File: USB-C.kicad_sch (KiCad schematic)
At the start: 6 parts, among them J2 HRO_TYPE-C-31-M-12, U3 SRV05-4

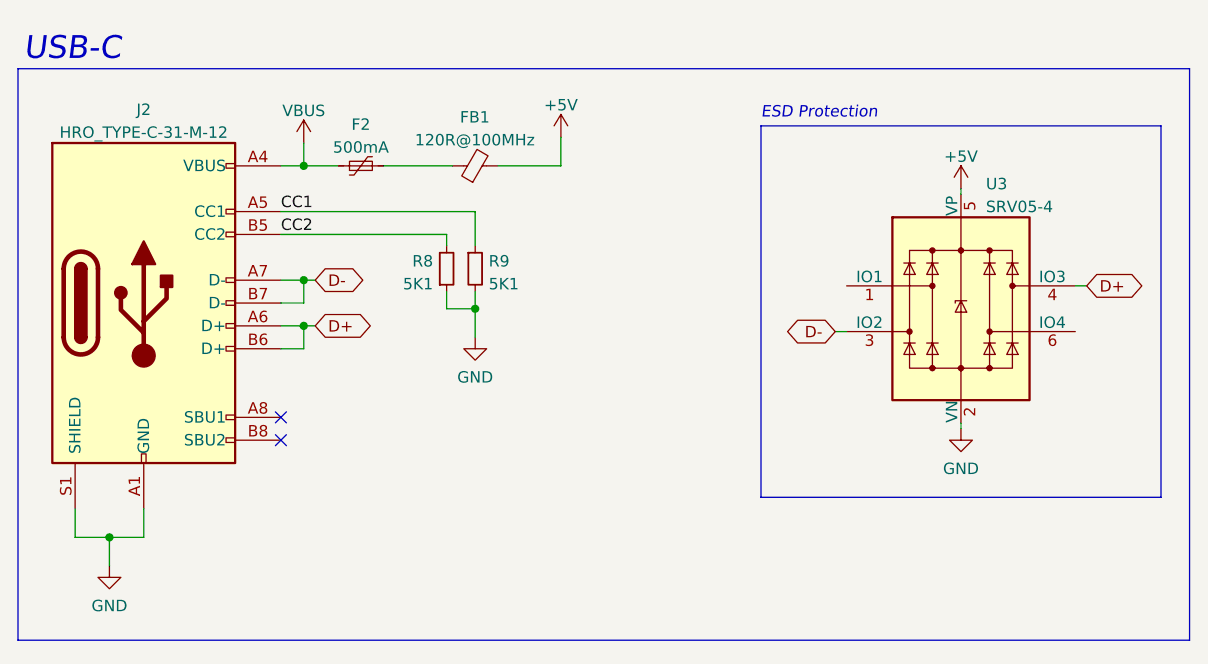
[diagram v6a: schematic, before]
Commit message: feat(schematic): Add titles and individual sheet comments
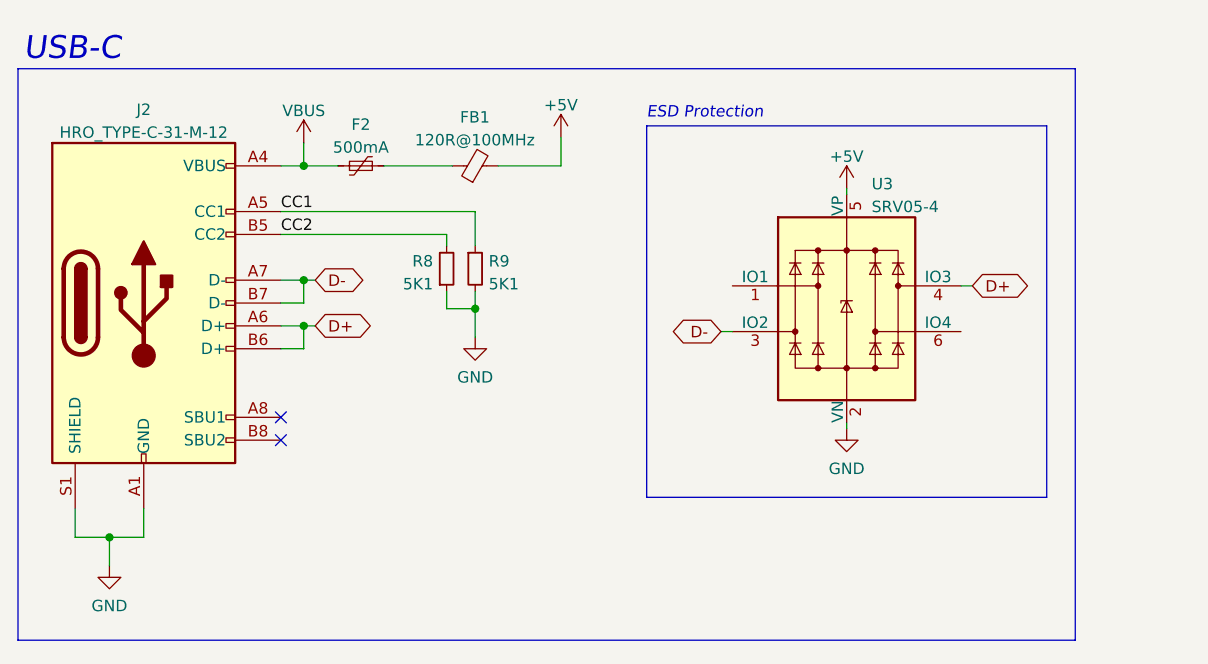
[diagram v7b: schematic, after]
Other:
- company: (none) -> Kurtis Lew
- title: (none) -> Conejo nRF52840 Keyboard - USB-C
- moved on the sheet: U3
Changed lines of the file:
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@@
 (kicad_sch (version 20211123) (generator eeschema)
   (paper "USLetter")
+  (title_block
+    (title "Conejo nRF52840 Keyboard - USB-C")
+    (company "Kurtis Lew")
+  )
   (junction (at 44.45 47.625) (diameter 0) (color 0 0 0 0)
   )
@@
   (no_connect (at 41.91 60.325))
   (no_connect (at 41.91 57.785))
-  (polyline (pts (xy 139.7 25.4) (xy 139.7 66.675))
-    (stroke (width 0) (type default) (color 0 0 0 0))
-  )
-  (wire (pts (xy 117.475 58.42) (xy 117.475 59.055))
+  (polyline (pts (xy 127 25.4) (xy 127 66.675))
+    (stroke (width 0) (type default) (color 0 0 0 0))
+  )
+  (wire (pts (xy 104.775 58.42) (xy 104.775 59.055))
     (stroke (width 0) (type default) (color 0 0 0 0))
   )
@@
     (stroke (width 0) (type default) (color 0 0 0 0))
   )
-  (wire (pts (xy 130.175 43.18) (xy 131.445 43.18))
-    (stroke (width 0) (type default) (color 0 0 0 0))
-  )
-  (polyline (pts (xy 142.875 19.05) (xy 142.875 82.55))
+  (wire (pts (xy 117.475 43.18) (xy 118.745 43.18))
+    (stroke (width 0) (type default) (color 0 0 0 0))
+  )
+  (polyline (pts (xy 130.175 19.05) (xy 130.175 82.55))
     (stroke (width 0) (type default) (color 0 0 0 0))
   )
@@
     (stroke (width 0) (type default) (color 0 0 0 0))
   )
-  (polyline (pts (xy 142.875 82.55) (xy 12.7 82.55))
+  (polyline (pts (xy 130.175 82.55) (xy 12.7 82.55))
     (stroke (width 0) (type default) (color 0 0 0 0))
   )
@@
     (stroke (width 0) (type default) (color 0 0 0 0))
   )
-  (polyline (pts (xy 95.25 66.675) (xy 95.25 25.4))
+  (polyline (pts (xy 82.55 66.675) (xy 82.55 25.4))
     (stroke (width 0) (type default) (color 0 0 0 0))
   )
@@
     (stroke (width 0) (type default) (color 0 0 0 0))
   )
-  (wire (pts (xy 104.775 48.26) (xy 103.505 48.26))
+  (wire (pts (xy 92.075 48.26) (xy 90.805 48.26))
     (stroke (width 0) (type default) (color 0 0 0 0))
   )
@@
     (stroke (width 0) (type default) (color 0 0 0 0))
   )
-  (wire (pts (xy 117.475 32.385) (xy 117.475 33.02))
+  (wire (pts (xy 104.775 32.385) (xy 104.775 33.02))
     (stroke (width 0) (type default) (color 0 0 0 0))
   )
@@
     (stroke (width 0) (type default) (color 0 0 0 0))
   )
-  (polyline (pts (xy 139.7 66.675) (xy 95.25 66.675))
+  (polyline (pts (xy 127 66.675) (xy 82.55 66.675))
     (stroke (width 0) (type default) (color 0 0 0 0))
   )
@@
     (stroke (width 0) (type default) (color 0 0 0 0))
   )
-  (polyline (pts (xy 95.25 25.4) (xy 139.7 25.4))
+  (polyline (pts (xy 82.55 25.4) (xy 127 25.4))
     (stroke (width 0) (type default) (color 0 0 0 0))
   )
@@
     (stroke (width 0) (type default) (color 0 0 0 0))
   )
-  (polyline (pts (xy 12.7 19.05) (xy 142.875 19.05))
+  (polyline (pts (xy 12.7 19.05) (xy 130.175 19.05))
     (stroke (width 0) (type default) (color 0 0 0 0))
   )
@@
     (stroke (width 0) (type default) (color 0 0 0 0))
   )
-  (text "ESD Protection\n" (at 95.25 24.765 0)
+  (text "ESD Protection\n" (at 82.55 24.765 0)
     (effects (font (size 1.27 1.27) italic) (justify left bottom))
   )
@@
     )
   )
-  (global_label "D+" (shape bidirectional) (at 131.445 43.18 0) (fields_autoplaced)
+  (global_label "D+" (shape bidirectional) (at 118.745 43.18 0) (fields_autoplaced)
     (effects (font (size 1.27 1.27)) (justify left))
-    (property "Intersheet References" "${INTERSHEET_REFS}" (id 0) (at 136.7005 43.1006 0)
+    (property "Intersheet References" "${INTERSHEET_REFS}" (id 0) (at 124.0005 43.1006 0)
       (effects (font (size 1.27 1.27)) (justify left) hide)
     )
   )
-  (global_label "D-" (shape bidirectional) (at 103.505 48.26 180) (fields_autoplaced)
+  (global_label "D-" (shape bidirectional) (at 90.805 48.26 180) (fields_autoplaced)
     (effects (font (size 1.27 1.27)) (justify right))
-    (property "Intersheet References" "${INTERSHEET_REFS}" (id 0) (at 98.2495 48.3394 0)
+    (property "Intersheet References" "${INTERSHEET_REFS}" (id 0) (at 85.5495 48.3394 0)
       (effects (font (size 1.27 1.27)) (justify right) hide)
     )
@@
     (pin "1")
   )
-  (symbol (lib_id "power:GND") (at 117.475 59.055 0) (unit 1)
+  (symbol (lib_id "power:GND") (at 104.775 59.055 0) (unit 1)
     (in_bom yes) (on_board yes)
-    (property "Reference" "#PWR0116" (id 0) (at 117.475 65.405 0)
-      (effects (font (size 1.27 1.27)) hide)
-    )
-    (property "Value" "GND" (id 1) (at 117.475 63.4984 0))
-    (property "Footprint" "" (id 2) (at 117.475 59.055 0)
-      (effects (font (size 1.27 1.27)) hide)
-    )
-    (property "Datasheet" "" (id 3) (at 117.475 59.055 0)
-      (effects (font (size 1.27 1.27)) hide)
-    )
-    (pin "1")
-  )
-  (symbol (lib_id "Power_Protection:SRV05-4") (at 117.475 45.72 0) (unit 1)
-    (in_bom yes) (on_board yes) (fields_autoplaced)
-    (property "Reference" "U3" (id 0) (at 120.2437 31.8602 0)
-      (effects (font (size 1.27 1.27)) (justify left))
-    )
-    (property "Value" "SRV05-4" (id 1) (at 120.2437 34.3971 0)
-      (effects (font (size 1.27 1.27)) (justify left))
-    )
-    (property "Footprint" "marbastlib-various:SOT-23-6-routable" (id 2) (at 135.255 57.15 0)
-      (effects (font (size 1.27 1.27)) hide)
-    )
-    (property "Datasheet" "http://www.onsemi.com/pub/Collateral/SRV05-4-D.PDF" (id 3) (at 117.475 45.72 0)
+    (property "Reference" "#PWR0116" (id 0) (at 104.775 65.405 0)
+      (effects (font (size 1.27 1.27)) hide)
+    )
+    (property "Value" "GND" (id 1) (at 104.775 63.4984 0))
+    (property "Footprint" "" (id 2) (at 104.775 59.055 0)
+      (effects (font (size 1.27 1.27)) hide)
+    )
+    (property "Datasheet" "" (id 3) (at 104.775 59.055 0)
+      (effects (font (size 1.27 1.27)) hide)
+    )
+    (pin "1")
+  )
+  (symbol (lib_id "Power_Protection:SRV05-4") (at 104.775 45.72 0) (unit 1)
+    (in_bom yes) (on_board yes) (fields_autoplaced)
+    (property "Reference" "U3" (id 0) (at 107.5437 31.8602 0)
+      (effects (font (size 1.27 1.27)) (justify left))
+    )
+    (property "Value" "SRV05-4" (id 1) (at 107.5437 34.3971 0)
+      (effects (font (size 1.27 1.27)) (justify left))
+    )
+    (property "Footprint" "marbastlib-various:SOT-23-6-routable" (id 2) (at 122.555 57.15 0)
+      (effects (font (size 1.27 1.27)) hide)
+    )
+    (property "Datasheet" "http://www.onsemi.com/pub/Collateral/SRV05-4-D.PDF" (id 3) (at 104.775 45.72 0)
       (effects (font (size 1.27 1.27)) hide)
     )
@@
     (pin "2")
   )
-  (symbol (lib_id "power:+5V") (at 117.475 32.385 0) (unit 1)
-    (in_bom yes) (on_board yes) (fields_autoplaced)
-    (property "Reference" "#PWR0114" (id 0) (at 117.475 36.195 0)
-      (effects (font (size 1.27 1.27)) hide)
-    )
-    (property "Value" "+5V" (id 1) (at 117.475 28.8092 0))
-    (property "Footprint" "" (id 2) (at 117.475 32.385 0)
-      (effects (font (size 1.27 1.27)) hide)
-    )
-    (property "Datasheet" "" (id 3) (at 117.475 32.385 0)
-      (effects (font (size 1.27 1.27)) hide)
-    )
+  (symbol (lib_id "power:+5V") (at 104.775 32.385 0) (unit 1)
+    (in_bom yes) (on_board yes) (fields_autoplaced)
+    (property "Reference" "#PWR0114" (id 0) (at 104.775 36.195 0)
+      (effects (font (size 1.27 1.27)) hide)
+    )
+    (property "Value" "+5V" (id 1) (at 104.775 28.8092 0))
+    (property "Footprint" "" (id 2) (at 104.775 32.385 0)
+      (effects (font (size 1.27 1.27)) hide)
+    )
+    (property "Datasheet" "" (id 3) (at 104.775 32.385 0)
+      (effects (font (size 1.27 1.27)) hide)
+    )

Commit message: feat(pcb): Version 0.4
- Prepare to move from JLC7628 stackup to JLC3313 stackup (Lowers dielectric constant from 4.6 to 4.05)
- Increase mounting hole diameter back to 5.4mm
- 6mil signals, 10mil power, 13 mil vias
  - 3W spacing wherever possible
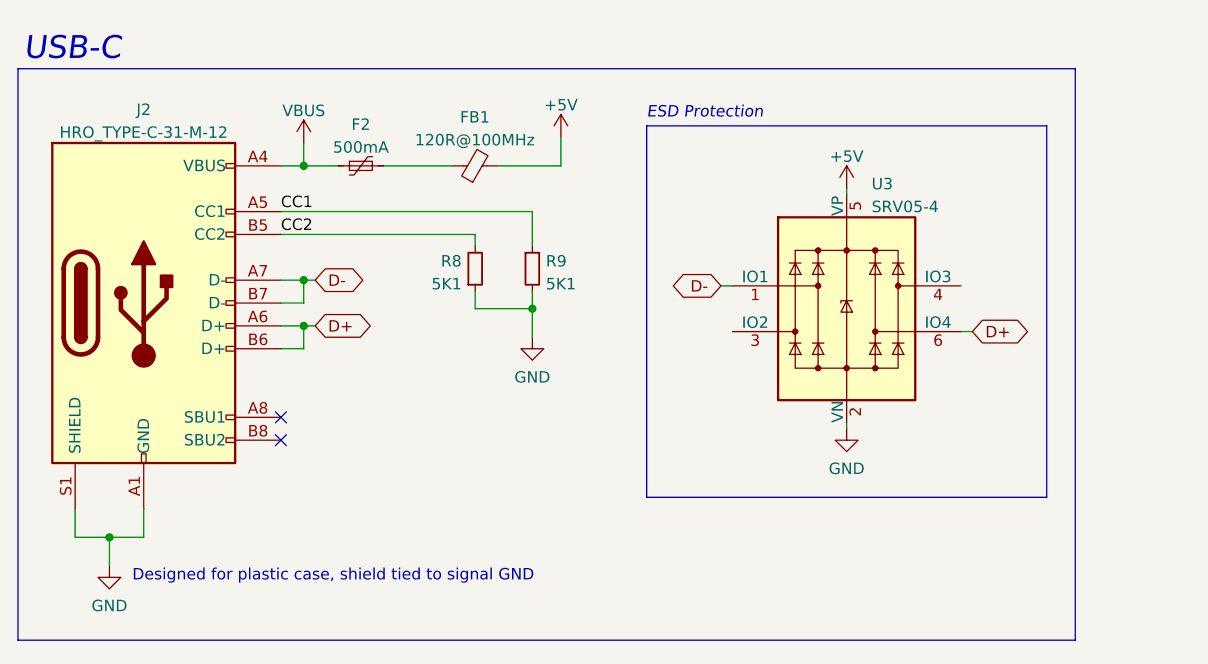
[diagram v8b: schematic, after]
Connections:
- net D+: now also U3.6 (IO4); no longer U3.4 (IO3)
- net D-: now also U3.1 (IO1); no longer U3.3 (IO2)
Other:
- note added: "Designed for plastic case, shield tied to signal GND"
- moved on the sheet: R8, R9
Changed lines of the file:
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@@
   (junction (at 44.45 42.545) (diameter 0) (color 0 0 0 0)
   )
-  (junction (at 63.5 45.72) (diameter 0) (color 0 0 0 0)
+  (junction (at 69.85 45.72) (diameter 0) (color 0 0 0 0)
   )
   (junction (at 44.45 29.845) (diameter 0) (color 0 0 0 0)
@@
     (stroke (width 0) (type default) (color 0 0 0 0))
   )
-  (wire (pts (xy 117.475 43.18) (xy 118.745 43.18))
+  (wire (pts (xy 117.475 48.26) (xy 118.745 48.26))
     (stroke (width 0) (type default) (color 0 0 0 0))
   )
@@
     (stroke (width 0) (type default) (color 0 0 0 0))
   )
-  (wire (pts (xy 60.325 37.465) (xy 60.325 38.735))
+  (wire (pts (xy 63.5 37.465) (xy 63.5 38.735))
     (stroke (width 0) (type default) (color 0 0 0 0))
   )
@@
     (stroke (width 0) (type default) (color 0 0 0 0))
   )
-  (wire (pts (xy 60.325 43.815) (xy 60.325 45.72))
+  (wire (pts (xy 63.5 43.815) (xy 63.5 45.72))
     (stroke (width 0) (type default) (color 0 0 0 0))
   )
@@
     (stroke (width 0) (type default) (color 0 0 0 0))
   )
-  (wire (pts (xy 41.91 37.465) (xy 60.325 37.465))
+  (wire (pts (xy 41.91 37.465) (xy 63.5 37.465))
     (stroke (width 0) (type default) (color 0 0 0 0))
   )
@@
     (stroke (width 0) (type default) (color 0 0 0 0))
   )
-  (wire (pts (xy 92.075 48.26) (xy 90.805 48.26))
+  (wire (pts (xy 92.075 43.18) (xy 90.805 43.18))
     (stroke (width 0) (type default) (color 0 0 0 0))
   )
@@
     (stroke (width 0) (type default) (color 0 0 0 0))
   )
-  (wire (pts (xy 63.5 34.925) (xy 63.5 38.735))
+  (wire (pts (xy 69.85 34.925) (xy 69.85 38.735))
     (stroke (width 0) (type default) (color 0 0 0 0))
   )
@@
     (stroke (width 0) (type default) (color 0 0 0 0))
   )
-  (wire (pts (xy 63.5 43.815) (xy 63.5 45.72))
-    (stroke (width 0) (type default) (color 0 0 0 0))
-  )
-  (wire (pts (xy 41.91 34.925) (xy 63.5 34.925))
+  (wire (pts (xy 69.85 43.815) (xy 69.85 45.72))
+    (stroke (width 0) (type default) (color 0 0 0 0))
+  )
+  (wire (pts (xy 41.91 34.925) (xy 69.85 34.925))
     (stroke (width 0) (type default) (color 0 0 0 0))
   )
@@
     (stroke (width 0) (type default) (color 0 0 0 0))
   )
-  (wire (pts (xy 60.325 45.72) (xy 63.5 45.72))
-    (stroke (width 0) (type default) (color 0 0 0 0))
-  )
-  (wire (pts (xy 63.5 48.895) (xy 63.5 45.72))
-    (stroke (width 0) (type default) (color 0 0 0 0))
+  (wire (pts (xy 63.5 45.72) (xy 69.85 45.72))
+    (stroke (width 0) (type default) (color 0 0 0 0))
+  )
+  (wire (pts (xy 69.85 48.895) (xy 69.85 45.72))
+    (stroke (width 0) (type default) (color 0 0 0 0))
+  )
+  (text "Designed for plastic case, shield tied to signal GND"
+    (at 25.4 76.2 0)
+    (effects (font (size 1.27 1.27)) (justify left bottom))
   )
   (text "ESD Protection\n" (at 82.55 24.765 0)
@@
     )
   )
-  (global_label "D+" (shape bidirectional) (at 118.745 43.18 0) (fields_autoplaced)
+  (global_label "D+" (shape bidirectional) (at 118.745 48.26 0) (fields_autoplaced)
     (effects (font (size 1.27 1.27)) (justify left))
-    (property "Intersheet References" "${INTERSHEET_REFS}" (id 0) (at 124.0005 43.1006 0)
+    (property "Intersheet References" "${INTERSHEET_REFS}" (id 0) (at 124.0005 48.1806 0)
       (effects (font (size 1.27 1.27)) (justify left) hide)
     )
   )
-  (global_label "D-" (shape bidirectional) (at 90.805 48.26 180) (fields_autoplaced)
+  (global_label "D-" (shape bidirectional) (at 90.805 43.18 180) (fields_autoplaced)
     (effects (font (size 1.27 1.27)) (justify right))
-    (property "Intersheet References" "${INTERSHEET_REFS}" (id 0) (at 85.5495 48.3394 0)
+    (property "Intersheet References" "${INTERSHEET_REFS}" (id 0) (at 85.5495 43.2594 0)
       (effects (font (size 1.27 1.27)) (justify right) hide)
     )
@@
     )
   )
-  (symbol (lib_id "power:GND") (at 63.5 48.895 0) (unit 1)
-    (in_bom yes) (on_board yes) (fields_autoplaced)
-    (property "Reference" "#PWR0127" (id 0) (at 63.5 55.245 0)
-      (effects (font (size 1.27 1.27)) hide)
-    )
-    (property "Value" "GND" (id 1) (at 63.5 53.3384 0))
-    (property "Footprint" "" (id 2) (at 63.5 48.895 0)
-      (effects (font (size 1.27 1.27)) hide)
-    )
-    (property "Datasheet" "" (id 3) (at 63.5 48.895 0)
+  (symbol (lib_id "power:GND") (at 69.85 48.895 0) (unit 1)
+    (in_bom yes) (on_board yes) (fields_autoplaced)
+    (property "Reference" "#PWR0127" (id 0) (at 69.85 55.245 0)
+      (effects (font (size 1.27 1.27)) hide)
+    )
+    (property "Value" "GND" (id 1) (at 69.85 53.3384 0))
+    (property "Footprint" "" (id 2) (at 69.85 48.895 0)
+      (effects (font (size 1.27 1.27)) hide)
+    )
+    (property "Datasheet" "" (id 3) (at 69.85 48.895 0)
       (effects (font (size 1.27 1.27)) hide)
     )
@@
     (pin "6")
   )
-  (symbol (lib_id "Device:R_Small") (at 63.5 41.275 0) (unit 1)
-    (in_bom yes) (on_board yes) (fields_autoplaced)
-    (property "Reference" "R9" (id 0) (at 64.9986 40.4403 0)
+  (symbol (lib_id "Device:R_Small") (at 69.85 41.275 0) (unit 1)
+    (in_bom yes) (on_board yes) (fields_autoplaced)
+    (property "Reference" "R9" (id 0) (at 71.3486 40.4403 0)
       (effects (font (size 1.27 1.27)) (justify left))
     )
-    (property "Value" "5K1" (id 1) (at 64.9986 42.9772 0)
+    (property "Value" "5K1" (id 1) (at 71.3486 42.9772 0)
       (effects (font (size 1.27 1.27)) (justify left))
     )
-    (property "Footprint" "Resistor_SMD:R_0402_1005Metric" (id 2) (at 63.5 41.275 0)
-      (effects (font (size 1.27 1.27)) hide)
-    )
-    (property "Datasheet" "~" (id 3) (at 63.5 41.275 0)
+    (property "Footprint" "Resistor_SMD:R_0402_1005Metric" (id 2) (at 69.85 41.275 0)
+      (effects (font (size 1.27 1.27)) hide)
+    )
+    (property "Datasheet" "~" (id 3) (at 69.85 41.275 0)
       (effects (font (size 1.27 1.27)) hide)
     )
@@
     (pin "1")
   )
-  (symbol (lib_id "Device:R_Small") (at 60.325 41.275 0) (mirror x) (unit 1)
-    (in_bom yes) (on_board yes) (fields_autoplaced)
-    (property "Reference" "R8" (id 0) (at 58.8264 40.4403 0)
+  (symbol (lib_id "Device:R_Small") (at 63.5 41.275 0) (mirror x) (unit 1)
+    (in_bom yes) (on_board yes) (fields_autoplaced)
+    (property "Reference" "R8" (id 0) (at 62.0014 40.4403 0)
       (effects (font (size 1.27 1.27)) (justify right))
     )
-    (property "Value" "5K1" (id 1) (at 58.8264 42.9772 0)
+    (property "Value" "5K1" (id 1) (at 62.0014 42.9772 0)
       (effects (font (size 1.27 1.27)) (justify right))
     )
-    (property "Footprint" "Resistor_SMD:R_0402_1005Metric" (id 2) (at 60.325 41.275 0)
-      (effects (font (size 1.27 1.27)) hide)
-    )
-    (property "Datasheet" "~" (id 3) (at 60.325 41.275 0)
-      (effects (font (size 1.27 1.27)) hide)
-    )
+    (property "Footprint" "Resistor_SMD:R_0402_1005Metric" (id 2) (at 63.5 41.275 0)
+      (effects (font (size 1.27 1.27)) hide)
+    )
+    (property "Datasheet" "~" (id 3) (at 63.5 41.275 0)
+      (effects (font (size 1.27 1.27)) hide)
+    )
